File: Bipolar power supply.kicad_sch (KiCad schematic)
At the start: 30 parts, among them J1 Screw 6-32, J2 Screw 6-32, J3 Screw 6-32, J4 Conn_01x03, U1 LM317_TO-220, U2 LM337_TO-220

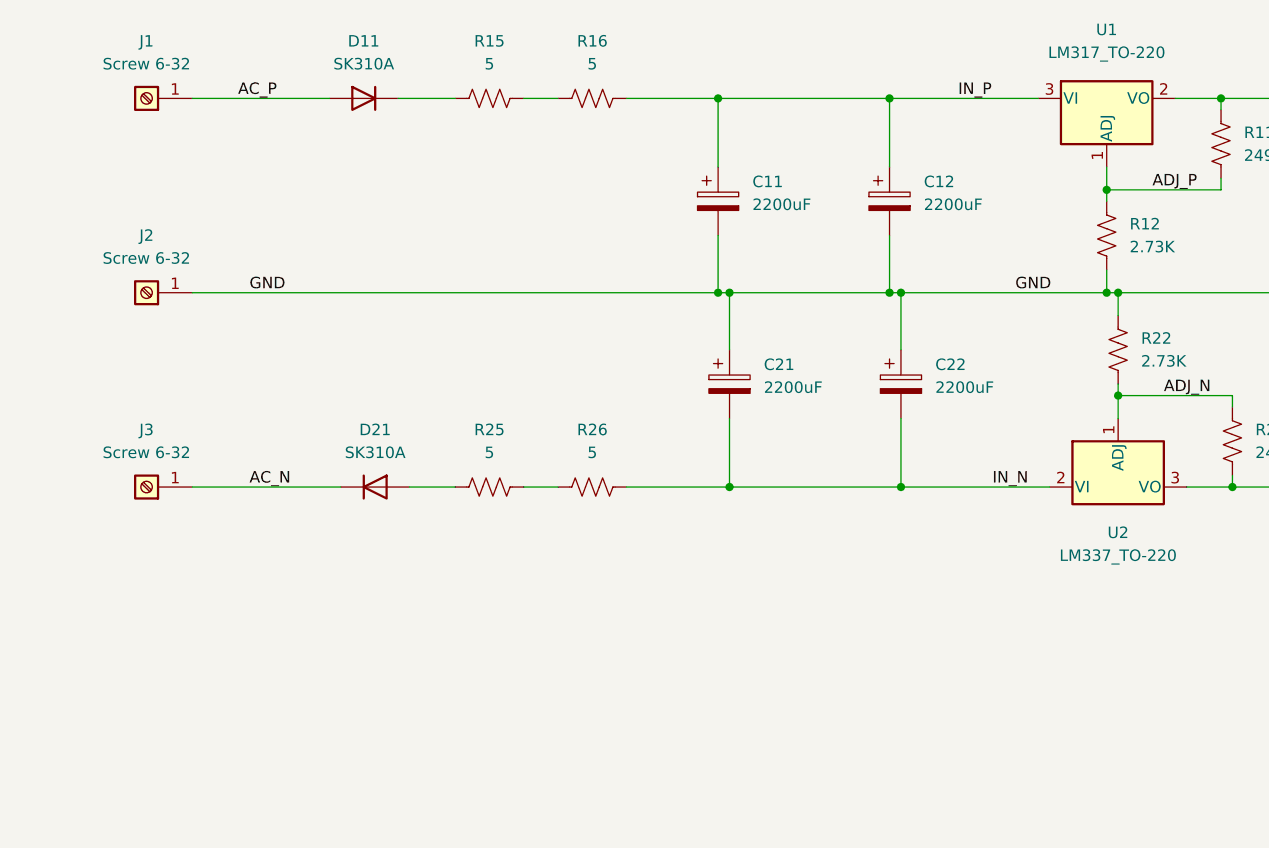
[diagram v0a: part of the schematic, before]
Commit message: Revised schematic for (1) bridge rectifiers, (2) three power resistors, and (3) fuse holders.
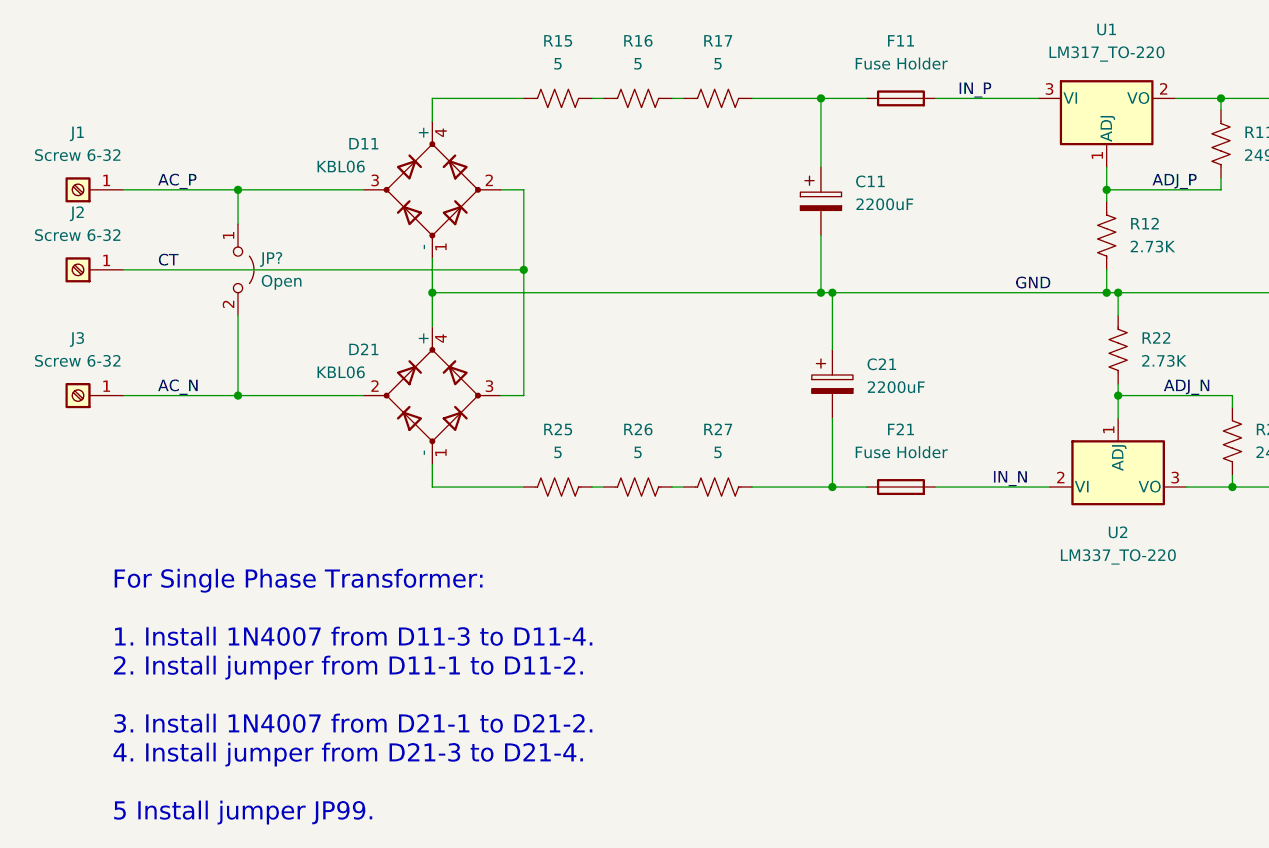
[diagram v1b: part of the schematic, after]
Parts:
- removed C12, C22: 2200uF, Capacitor_THT:CP_Radial_D16.0mm_P7.50mm, symbol Device:C_Polarized
- removed D11, D21: SK310A, Diode_SMD:D_SMA_Handsoldering, symbol Device:D
- added D11, D21: KBL06, Diode_THT:Diode_Bridge_Vishay_KBL, symbol Device:D_Bridge_-AA+
- added F11, F21: Fuse Holder, $Local:FuseHolder_6.8x19.8mm_P3.4x13.5mm_Vetical, symbol Device:Fuse
- added JP?: Open, $Local:Jumper_P25.40mm, symbol Jumper:Jumper_2_Open
- added R17, R27: 5, $Local:R_Axial_L25.5mm_D8.7mm_P30.48mm_Horizontal, symbol Device:R_US
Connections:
- net AC_N: now also D21.2, JP?.2 (B)
- net AC_P: now also D11.3, JP?.1 (A)
- net GND: now also D11.1 (-), D21.4 (+); no longer J2.1 (Pin_1)
- net IN_N: now also F21.2; no longer C21.2, R26.2
- net IN_P: now also F11.2; no longer C11.1, R16.2
- net at R25.1: now also D21.1 (-)
- net at R15.1: now also D11.4 (+)
- new net: C11.1, F11.1, R17.2
- new net: R16.2, R17.1
- new net: C21.2, F21.1, R27.2
- new net: R26.2, R27.1
- new net CT: D11.2, D21.3, J2.1 (Pin_1)
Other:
- note added: "For Single Phase Transformer: 1. Install 1N4007 from D11-3 to D11-4. 2. Install jumper from D11-1 to D11-2. 3. Install 1N4007 from D21-1 to D21-2. 4. Install jumper from D21-3 to D21-4. 5 Install jumper JP99."
- moved on the sheet: C11, C21, J1, J2, J3, R15, R16, R25, R26

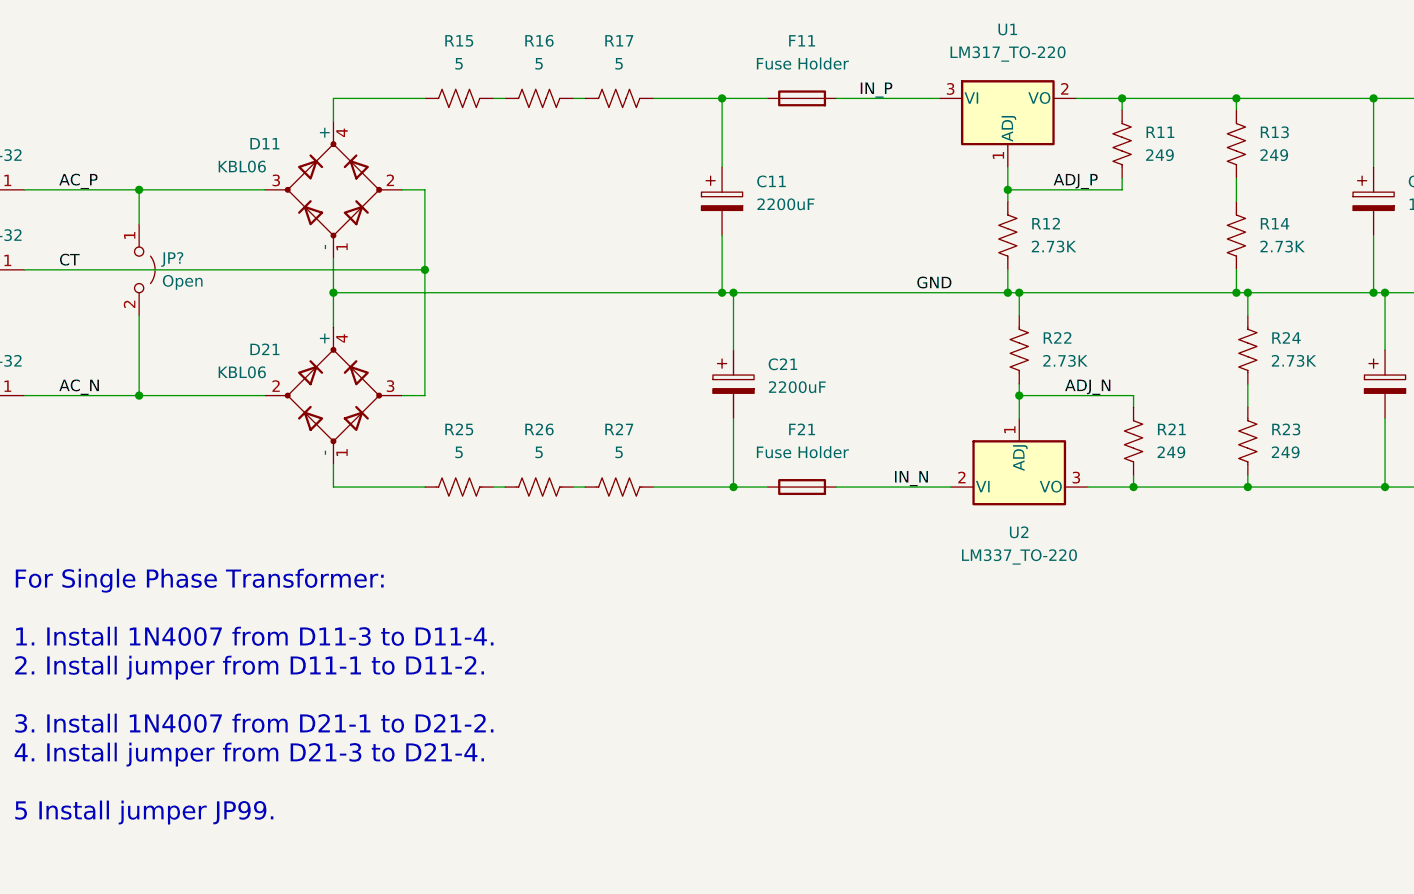
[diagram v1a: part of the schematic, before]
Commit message: First pass at routing in 70x100 mm panel.
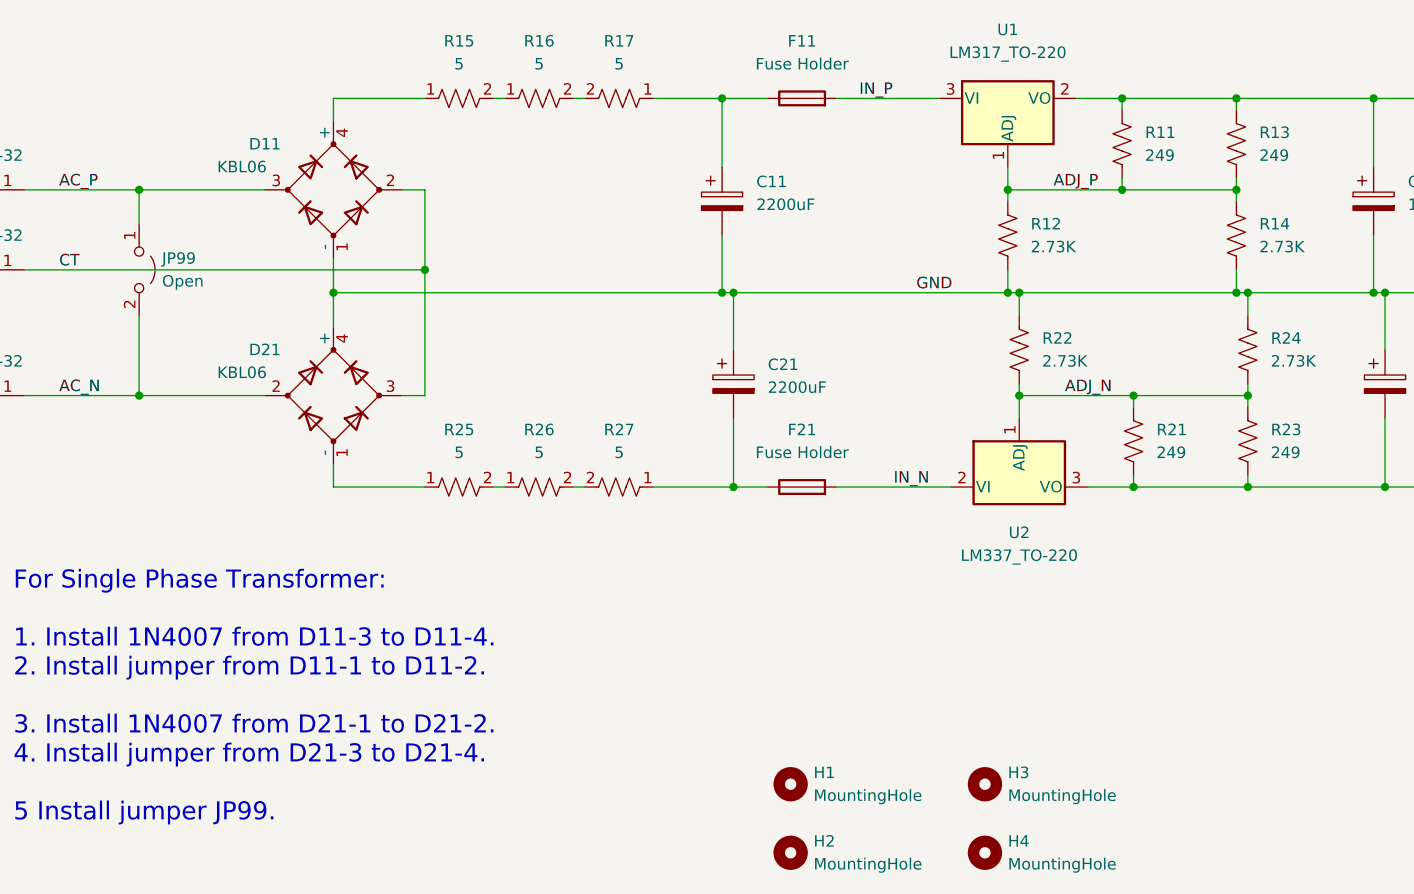
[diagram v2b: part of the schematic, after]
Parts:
- added H1, H2, H3, H4: MountingHole, MountingHole:MountingHole_3.5mm_Pad, symbol Mechanical:MountingHole
- R15, R16, R17, R25, R26, R27: footprint $Local:R_Axial_L25.5mm_D8.7mm_P30.48mm_Horizontal -> Resistor_THT:R_Axial_DIN0614_L14.3mm_D5.7mm_P15.24mm_Horizontal
- gave numbers to parts that had none: 1
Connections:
- net ADJ_N: now also R23.1, R24.2
- net ADJ_P: now also R13.2, R14.1
- net at C11.1, F11.1: now also R17.1; no longer R17.2
- net at R16.2: now also R17.2; no longer R17.1
- net at C21.2, F21.1: now also R27.1; no longer R27.2
- net at R26.2: now also R27.2; no longer R27.1

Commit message: Created footprint for TO-220 with Heatsink
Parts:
- U1, U2: footprint Package_TO_SOT_THT:TO-220-3_Vertical -> $Local:TO-220-3_Vertical_Heatsink_19.1x9.7mm
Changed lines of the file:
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@@
     (property "Reference" "U2" (id 0) (at 151.13 92.71 0))
     (property "Value" "LM337_TO-220" (id 1) (at 151.13 95.25 0))
-    (property "Footprint" "Package_TO_SOT_THT:TO-220-3_Vertical" (id 2) (at 151.13 92.71 0)
+    (property "Footprint" "$Local:TO-220-3_Vertical_Heatsink_19.1x9.7mm" (id 2) (at 151.13 92.71 0)
       (effects (font (size 1.27 1.27) italic) hide)
     )
@@
     (property "Reference" "U1" (id 0) (at 149.86 36.83 0))
     (property "Value" "LM317_TO-220" (id 1) (at 149.86 39.37 0))
-    (property "Footprint" "Package_TO_SOT_THT:TO-220-3_Vertical" (id 2) (at 149.86 38.1 0)
+    (property "Footprint" "$Local:TO-220-3_Vertical_Heatsink_19.1x9.7mm" (id 2) (at 149.86 38.1 0)
       (effects (font (size 1.27 1.27) italic) hide)
     )
@@
     )
     (path "/dfa102b1-17da-44f4-a9e1-ead862583975"
-      (reference "U1") (unit 1) (value "LM317_TO-220") (footprint "Package_TO_SOT_THT:TO-220-3_Vertical")
+      (reference "U1") (unit 1) (value "LM317_TO-220") (footprint "$Local:TO-220-3_Vertical_Heatsink_19.1x9.7mm")
     )
     (path "/3e937f05-29c9-490d-9909-b5647b1fa632"
-      (reference "U2") (unit 1) (value "LM337_TO-220") (footprint "Package_TO_SOT_THT:TO-220-3_Vertical")
-    )
-  )
+      (reference "U2") (unit 1) (value "LM337_TO-220") (footprint "$Local:TO-220-3_Vertical_Heatsink_19.1x9.7mm")
+    )
+  )

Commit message: Routing WIP.
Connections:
- net at C11.1, F11.1: now also R17.2; no longer R17.1
- net at R16.2: now also R17.1; no longer R17.2
- net at C21.2, F21.1: now also R27.2; no longer R27.1
- net at R26.2: now also R27.1; no longer R27.2
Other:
- moved on the sheet: R17, R27
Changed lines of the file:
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@@
     (pin "2")
   )
-  (symbol (lib_name "R_US_6") (lib_id "Device:R_US") (at 106.68 44.45 270) (unit 1)
+  (symbol (lib_name "R_US_6") (lib_id "Device:R_US") (at 106.68 44.45 90) (unit 1)
     (in_bom yes) (on_board yes) (fields_autoplaced)
     (property "Reference" "R17" (id 0) (at 106.68 38.1 90))
     (property "Value" "5" (id 1) (at 106.68 40.64 90))
-    (property "Footprint" "Resistor_THT:R_Axial_DIN0614_L14.3mm_D5.7mm_P15.24mm_Horizontal" (id 2) (at 106.426 45.466 90)
+    (property "Footprint" "Resistor_THT:R_Axial_DIN0614_L14.3mm_D5.7mm_P15.24mm_Horizontal" (id 2) (at 106.934 43.434 90)
       (effects (font (size 1.27 1.27)) hide)
     )
@@
     (pin "2")
   )
-  (symbol (lib_name "R_US_3") (lib_id "Device:R_US") (at 106.68 87.63 270) (unit 1)
+  (symbol (lib_name "R_US_3") (lib_id "Device:R_US") (at 106.68 87.63 90) (unit 1)
     (in_bom yes) (on_board yes) (fields_autoplaced)
     (property "Reference" "R27" (id 0) (at 106.68 81.28 90))
     (property "Value" "5" (id 1) (at 106.68 83.82 90))
-    (property "Footprint" "Resistor_THT:R_Axial_DIN0614_L14.3mm_D5.7mm_P15.24mm_Horizontal" (id 2) (at 106.426 88.646 90)
-      (effects (font (size 1.27 1.27)) hide)
-    )
+    (property "Footprint" "Resistor_THT:R_Axial_DIN0614_L14.3mm_D5.7mm_P15.24mm_Horizontal" (id 2) (at 106.934 86.614 90)
+      (effects (font (size 1.27 1.27)) hide)
+    )
